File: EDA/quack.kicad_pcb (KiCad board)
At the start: 2 copper layers, 56.6 x 57.7 mm, 39 parts, among them IC1 ESP32-PICO-D4, IC2 SN74LVC4245APWR, J1 DIN-4, J2 DB9_Male, J3 FTDI, J4 MODE, U1 AMS1117-3.3, U2 74LVC2T45DC

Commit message: PCB version 1.3
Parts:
- removed J4: MODE, Connector_PinHeader_2.54mm:PinHeader_2x03_P2.54mm_Vertical
- added Q1: LBSS84LT1G, Package_TO_SOT_SMD:SOT-23, F.Cu at (177.5, 101.0)
- added R6: 470, Resistor_SMD:R_0805_2012Metric, F.Cu at (181.0, 97.0)
- added R7: 470, Resistor_SMD:R_0805_2012Metric, F.Cu at (178.5, 97.0)
- added REF**: MountingHole_3.2mm_M3_Pad, MountingHole:MountingHole_3.2mm_M3_Pad, F.Cu at (169.3, 112.2)
- added REF**: MountingHole_3.2mm_M3_Pad, MountingHole:MountingHole_3.2mm_M3_Pad, F.Cu at (141.3, 112.2)
- added REF**: MountingHole_3.2mm_M3_Pad, MountingHole:MountingHole_3.2mm_M3_Pad, F.Cu at (169.3, 84.2)
- added REF**: MountingHole_3.2mm_M3_Pad, MountingHole:MountingHole_3.2mm_M3_Pad, F.Cu at (141.3, 84.2)
- added SW1: SW_DIP_x03, Button_Switch_THT:SW_DIP_SPSTx03_Slide_9.78x9.8mm_W7.62mm_P2.54mm, F.Cu at (180.5, 113.5)
- R1: value 68 -> 82
- R2, R3, R4: value 150 -> 330
- moved FB2 13.8 mm to (155.5, 111.5)
- moved U2 8.32 mm to (177.5, 105.5)
- moved C8 8.06 mm to (181.0, 104.0)
- moved C9 8.06 mm to (174.0, 104.0)
- moved TP1 7.91 mm to (169.5, 104.5)
- moved R3 3.00 mm to (171.5, 119.0)
- moved FB1 3.00 mm to (166.5, 119.1)
- moved R2 3.00 mm to (169.0, 119.1)
- moved C6 2.00 mm to (174.0, 97.0)
- moved FB3 1.46 mm to (153.0, 111.5), turned to 270 degrees
- moved G*** 0.50 mm to (144.0, 121.5)
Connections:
- IC1 pad 12: ADBSRC -> ~ADBHOST
- IC1 pad 13: BTOFF -> ~BTDIS
- IC1 pad 23: FLASH -> ~FLASH
- IC2 pad 21: GND -> ~ADBHOST
- IC2 pad 3: (no net) -> /quack_connectors/~ADBPULL
- U2 pad 4: (no net) -> GND
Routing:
- net BTOFF: track 90.1 -> 0.00 mm, vias 1 -> 0
- net ~BTDIS: track 0.00 -> 87.2 mm, vias 0 -> 1
- net ~ADBHOST: track 0.00 -> 47.8 mm, vias 0 -> 2
- net ADBSRC: track 38.6 -> 0.00 mm, vias 3 -> 0
- net ~FLASH: track 0.00 -> 28.8 mm, vias 0 -> 1
- net FLASH: track 25.8 -> 0.00 mm, vias 1 -> 0
- net +5V: track 130.8 -> 151.8 mm
- net Net-(FB1-Pad2): track 12.5 -> 30.8 mm
- net /quack_connectors/~ADBPULL: track 0.00 -> 16.3 mm
- net +3V3: track 127.0 -> 132.1 mm
- net DIR: track 36.8 -> 32.7 mm
- net Net-(Q1-Pad1): track 0.00 -> 3.94 mm
- net Net-(FB3-Pad2): track 7.28 -> 3.96 mm, vias 1 -> 0
- net Net-(IC1-Pad16): track 30.0 -> 26.9 mm
- net Net-(Q1-Pad2): track 0.00 -> 2.90 mm
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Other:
- board text added: "ADB Host"
- board text added: "Bluetooth Disable"
- board text removed: "ADBSrc"
- board text removed: "BTOff"

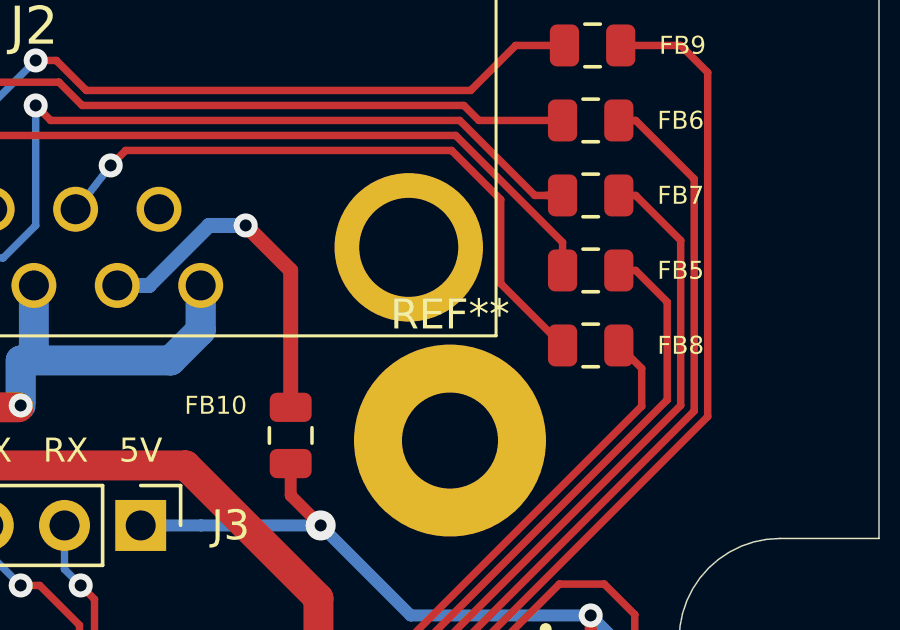
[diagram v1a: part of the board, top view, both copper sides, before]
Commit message: added mounting holes to schematic
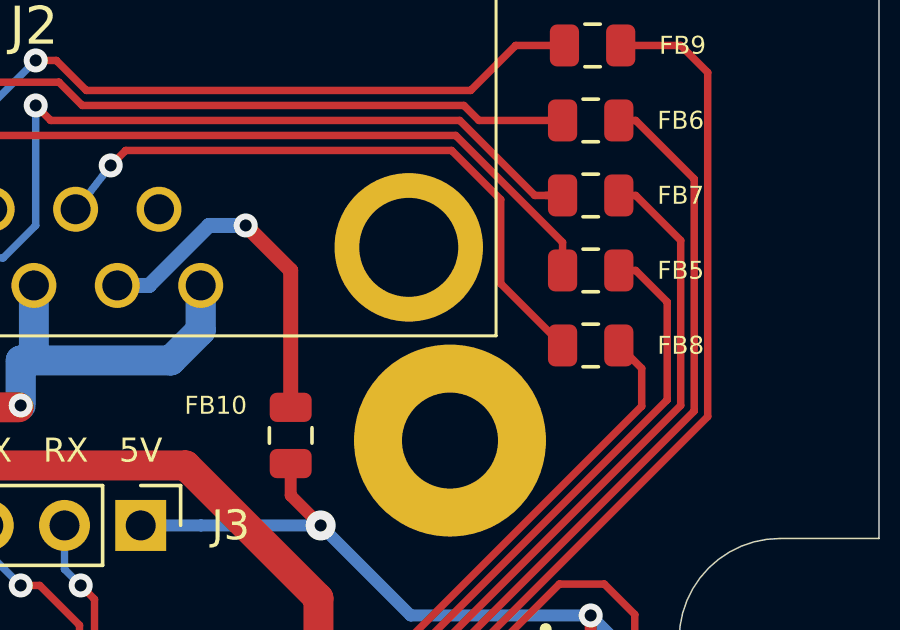
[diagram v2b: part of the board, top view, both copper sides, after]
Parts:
- removed REF** (x4): MountingHole_3.2mm_M3_Pad, MountingHole:MountingHole_3.2mm_M3_Pad
- added H1: M3, MountingHole:MountingHole_3.2mm_M3_Pad, F.Cu at (141.3, 84.2)
- added H2: M3, MountingHole:MountingHole_3.2mm_M3_Pad, F.Cu at (169.3, 84.2)
- added H3: M3, MountingHole:MountingHole_3.2mm_M3_Pad, F.Cu at (141.3, 112.2)
- added H4: M3, MountingHole:MountingHole_3.2mm_M3_Pad, F.Cu at (169.3, 112.2)

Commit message: PCB v1.4
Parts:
- added G***: LOGO, Macintosh logo:Macintosh logo, F.Cu at (132.7, 78.7)
- added H5: 1.152mm, MountingHole_Tooling:MountingHole_1.152mm, F.Cu at (130.2, 120.7)
- added H6: 1.152mm, MountingHole_Tooling:MountingHole_1.152mm, F.Cu at (181.0, 72.4)
- added R8: 22, Resistor_SMD:R_0805_2012Metric, F.Cu at (174.0, 108.0)
- added REF**: OSHW-Logo2_9.8x8mm_Copper, Symbol:OSHW-Logo2_9.8x8mm_Copper, B.Cu at (134.6, 121.3)
- R1: value 82 -> 150
- R2, R3, R4: value 330 -> 470
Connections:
- U2 pad 7: Net-(FB1-Pad2) -> Net-(R8-Pad2)
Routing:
- net Net-(R8-Pad2): track 0.00 -> 11.0 mm, vias 0 -> 2
- net Net-(FB1-Pad2): track 30.8 -> 37.2 mm
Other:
- board text added: "Michel "demik" Depeige :: 68kmla"
- board text added: "Quack Mouse Adapter REV 1.4"
- board text removed: "Michel "demik" Depeige 68kmla"
- board text removed: "Quack Mouse Adapter REV 1.3"

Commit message: fixed R1 and R4 values
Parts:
- R1: value 150 -> 470
- R4: value 470 -> 1200
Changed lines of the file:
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@@
   (title_block
     (title "Quack Mouse Adapter")
-    (date 2021-06-08)
+    (date 2021-08-15)
     (rev 1.4)
     (company Lostwave)
@@
       (effects (font (size 0.6 0.6) (thickness 0.15)))
     )
-    (fp_text value 150 (at 0 1.65 90) (layer F.Fab)
+    (fp_text value 470 (at 0 1.65 90) (layer F.Fab)
       (effects (font (size 1 1) (thickness 0.15)))
     )
@@
       (effects (font (size 0.6 0.6) (thickness 0.15)))
     )
-    (fp_text value 470 (at 0 1.65 90) (layer F.Fab)
-      (effects (font (size 1 1) (thickness 0.15)))
-    )
+    (fp_text value 1200 (at 0 1.65 90) (layer F.Fab)
+      (effects (font (size 1 1) (thickness 0.15)))
+    )

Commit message: PCB v1.5
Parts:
- removed IC1: ESP32-PICO-D4, ESP32-PICO-D4:ESP32-PICO-D4_1
- removed IC2: SN74LVC4245APWR, Package_SO:TSSOP-24_4.4x7.8mm_P0.65mm
- removed the REF** at (134.6, 121.3)
- added REF**: OSHW-Logo2_7.3x6mm_Copper, Symbol:OSHW-Logo2_7.3x6mm_Copper, B.Cu at (131.8, 111.2)
- added TP2: TestPoint DIR ESP32, TestPoint:TestPoint_Pad_1.0x1.0mm, F.Cu at (163.2, 97.0)
- added U3: ESP32-PICO-V3, Package_DFN_QFN:QFN-48-1EP_7x7mm_P0.5mm_EP5.3x5.3mm, F.Cu at (156.2, 97.8)
- added U4: SN74LVC4245APWR, Package_SO:TSSOP-24_4.4x7.8mm_P0.65mm, F.Cu at (168.5, 95.0)
- D1: value BLUE LED -> KT-0805B; footprint LED_SMD:LED_0805_2012Metric_Castellated -> LED_SMD:LED_0805_2012Metric
- D2: value YELLOW LED -> KT-0805Y; footprint LED_SMD:LED_0805_2012Metric_Castellated -> LED_SMD:LED_0805_2012Metric
- D3: value RED LED -> NCD0805R1; footprint LED_SMD:LED_0805_2012Metric_Castellated -> LED_SMD:LED_0805_2012Metric
- D4: value GREEN LED -> KT-0805G; footprint LED_SMD:LED_0805_2012Metric_Castellated -> LED_SMD:LED_0805_2012Metric
- FB1, FB2, FB3: value Ferrite_Bead -> GZ2012D601TF
- FB10, FB4, FB5, FB6, FB7, FB8, FB9: value Ferrite_Bead_Small -> GZ2012D601TF
- Q1: value LBSS84LT1G -> SI2301CDS-T1-GE3
- R1, R2, R3, R6, R7: value 470 -> 470Ω
- R4: value 1200 -> 1.5kΩ
- R5: value 10k -> 10kΩ
- R8: value 22 -> 22Ω
- U2: value 74LVC2T45DC -> SN74LVC2T45YZP; footprint Package_SO:VSSOP-8_2.3x2mm_P0.5mm -> Package_BGA:Texas_DSBGA-8_0.9x1.9mm_Layout2x4_P0.5mm
- moved G*** 0.25 mm to (144.0, 121.2)
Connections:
- C2 pad 1: +3V3 -> +3.3V
- C3 pad 1: +3V3 -> +3.3V
- C4 pad 1: +3V3 -> +3.3V
- C6 pad 1: +3V3 -> +3.3V
- C9 pad 2: +3V3 -> +3.3V
- J1 pad 2: (no net) -> unconnected-(J1-Pad2)
- J2 pad 6: (no net) -> unconnected-(J2-Pad6)
- R5 pad 1: +3V3 -> +3.3V
- R6 pad 2: /quack_connectors/~ADBPULL -> /quack_connectors/~{ADBPULL}
- R8 pad 2: Net-(R8-Pad2) -> Net-(U2-B1)
- SW1 pad 1: ~FLASH -> ~{FLASH}
- SW1 pad 2: ~BTDIS -> ~{BTDIS}
- SW1 pad 3: ~ADBHOST -> ~{ADBHOST}
- U1 pad 2: +3V3 -> +3.3V
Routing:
- net +3.3V: track 0.00 -> 132.6 mm, vias 0 -> 7
- net +3V3: track 132.1 -> 0.00 mm, vias 7 -> 0
- net ~BTDIS: track 87.2 -> 0.00 mm, vias 1 -> 0
- net ~{BTDIS}: track 0.00 -> 84.5 mm, vias 0 -> 1
- net ~ADBHOST: track 47.8 -> 0.00 mm, vias 2 -> 0
- net ~{ADBHOST}: track 0.00 -> 47.6 mm, vias 0 -> 2
- net ~{FLASH}: track 0.00 -> 32.4 mm, vias 0 -> 1
- net ~FLASH: track 28.8 -> 0.00 mm, vias 1 -> 0
- net ~OE: track 19.9 -> 0.00 mm
- net ~{OE}: track 0.00 -> 19.4 mm
- net /quack_connectors/~{ADBPULL}: track 0.00 -> 16.3 mm
- net /quack_connectors/~ADBPULL: track 16.3 -> 0.00 mm
- net Net-(R8-Pad2): track 11.0 -> 0.00 mm, vias 2 -> 0
- net Net-(U2-B1): track 0.00 -> 10.1 mm, vias 0 -> 2
- net Net-(Q1-D): track 37.2 -> 28.4 mm
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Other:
- net class +V removed
- net class Default removed
- net class GND removed
- rule pad_to_mask_clearance: 0.051 -> 0
- board text added: "Quack Mouse Adapter REV 1.5Q"
- board text removed: "Quack Mouse Adapter REV 1.4"
- board text removed: "•"

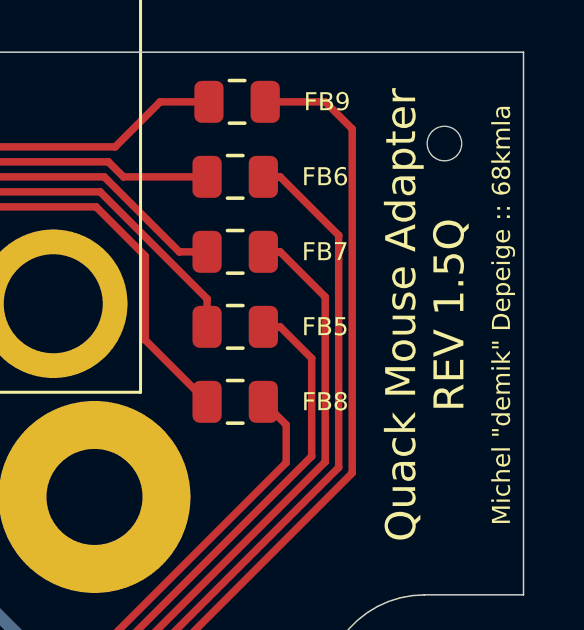
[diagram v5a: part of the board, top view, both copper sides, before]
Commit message: reverted PCB revision to 1.5
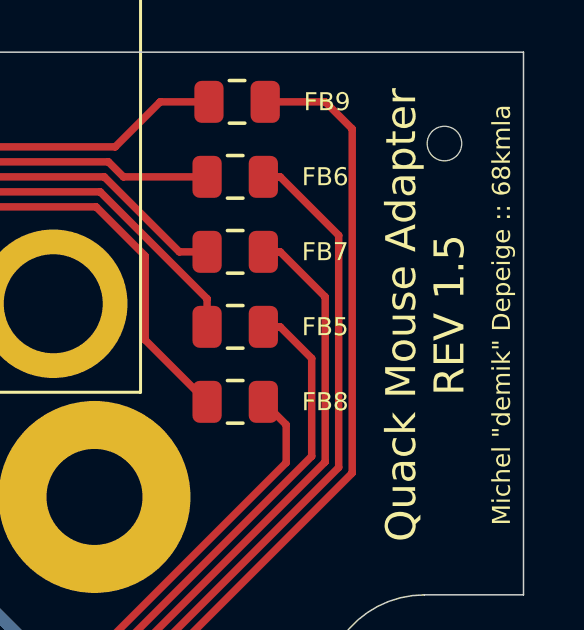
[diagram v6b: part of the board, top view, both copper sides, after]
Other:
- board text added: "Quack Mouse Adapter REV 1.5"
- board text removed: "Quack Mouse Adapter REV 1.5Q"
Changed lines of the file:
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@@
 		)
 	)
-	(gr_text "Quack Mouse Adapter\nREV 1.5Q"
+	(gr_text "Quack Mouse Adapter\nREV 1.5"
 		(at 180.34 78.105 90)
 		(layer "F.SilkS")

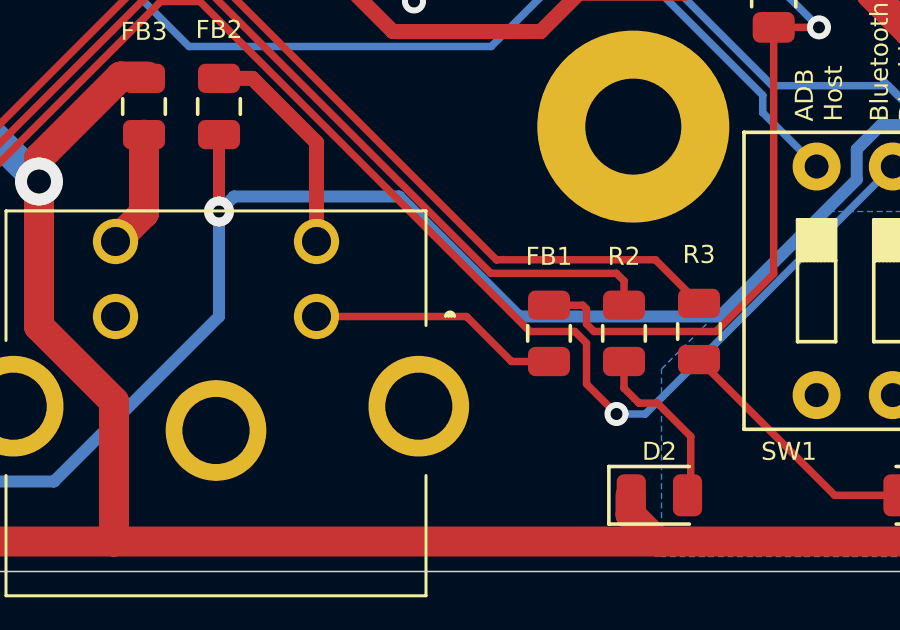
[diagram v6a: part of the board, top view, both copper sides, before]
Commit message: EDA lib: updated Mini DIN 4 connector
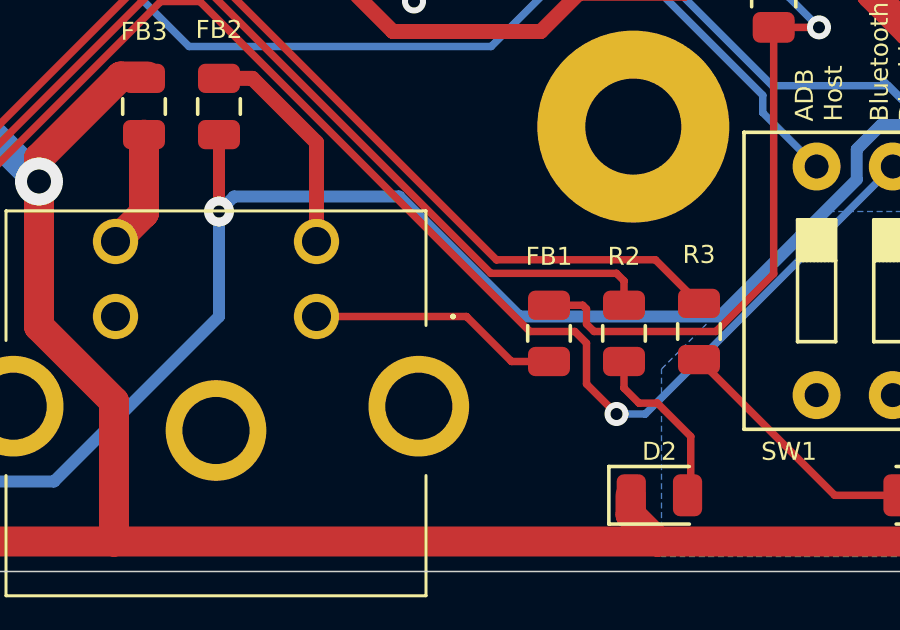
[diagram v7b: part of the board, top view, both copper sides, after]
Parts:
- J1: footprint Quack_MDIN4:57491811 -> Quack_MDIN4:5749181-1
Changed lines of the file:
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@@
 			)
 		)
-		(property "Datasheet" ""
+		(property "Datasheet" "~"
 			(at 0 0 270)
 			(layer "F.Fab")
@@
 		(embedded_fonts no)
 	)
-	(footprint "Quack_MDIN4:57491811"
+	(footprint "Quack_MDIN4:5749181-1"
 		(layer "F.Cu")
 		(at 158.75 118.5)
@@
 		(tags "Connector")
 		(property "Reference" "J1"
-			(at -3.35 0.75 0)
+			(at -3.25 0 0)
 			(layer "F.SilkS")
 			(hide yes)
@@
 		)
 		(fp_arc
-			(start 4.3 0)
-			(mid 4.45 -0.15)
+			(start 4.5 0)
+			(mid 4.55 -0.05)
 			(end 4.6 0)
 			(stroke
@@
 		)
 		(fp_arc
-			(start 4.4 0)
-			(mid 4.45 -0.05)
+			(start 4.6 0)
+			(mid 4.55 0.05)
 			(end 4.5 0)
 			(stroke
@@
 				(type solid)
 			)
-			(layer "Dwgs.User")
+			(layer "F.CrtYd")
 		)
 		(fp_line
@@
 				(type solid)
 			)
-			(layer "Dwgs.User")
+			(layer "F.CrtYd")
+		)
+		(fp_line
+			(start 6.088 -4.52)
+			(end -12.788 -4.52)
+			(stroke
+				(width 0.1)
+				(type solid)
+			)
+			(layer "F.CrtYd")
+		)
+		(fp_line
+			(start 6.088 10.31)
+			(end 6.088 -4.52)
+			(stroke
+				(width 0.1)
+				(type solid)
+			)
+			(layer "F.CrtYd")
 		)
 		(fp_line
@@
 				(type solid)
 			)
-			(layer "Dwgs.User")
+			(layer "F.Fab")
 		)
 		(fp_line
@@
 				(type solid)
 			)
-			(layer "Dwgs.User")
+			(layer "F.Fab")
 		)
 		(fp_line
@@
 				(type solid)
 			)
-			(layer "Dwgs.User")
+			(layer "F.Fab")
 		)
 		(fp_line
@@
 				(type solid)
 			)
-			(layer "Dwgs.User")
-		)
-		(fp_line
-			(start 6.088 -4.52)
-			(end -12.788 -4.52)
-			(stroke
-				(width 0.1)
-				(type solid)
-			)
-			(layer "Dwgs.User")
+			(layer "F.Fab")
 		)
-		(fp_line
-			(start 6.088 10.31)
-			(end 6.088 -4.52)
-			(stroke
-				(width 0.1)
-				(type solid)
+		(fp_text user "${REFERENCE}"
+			(at -3.35 2.895 0)
+			(layer "F.Fab")
+			(effects
+				(font
+					(size 1.27 1.27)
+					(thickness 0.254)
+				)
 			)
-			(layer "Dwgs.User")
 		)
 		(pad "1" thru_hole circle
-			(at 0 0 90)
+			(at 0 0)
 			(size 1.509 1.509)
 			(drill 0.97)
-			(layers "*.Cu" "*.Mask" "F.SilkS")
+			(layers "*.Cu" "*.Mask")
 			(remove_unused_layers no)
 			(net 20 "Net-(FB1-Pad1)")
@@
 		)
 		(pad "2" thru_hole circle
-			(at -6.7 0 90)
+			(at -6.7 0)
 			(size 1.509 1.509)
 			(drill 0.97)
-			(layers "*.Cu" "*.Mask" "F.SilkS")
+			(layers "*.Cu" "*.Mask")
 			(remove_unused_layers no)
 			(net 39 "unconnected-(J1-Pad2)")
@@
 		)
 		(pad "3" thru_hole circle
-			(at 0 -2.5 90)
+			(at 0 -2.5)
 			(size 1.509 1.509)
 			(drill 0.97)
-			(layers "*.Cu" "*.Mask" "F.SilkS")
+			(layers "*.Cu" "*.Mask")
 			(remove_unused_layers no)
 			(net 22 "Net-(FB2-Pad2)")
@@
 		)
 		(pad "4" thru_hole circle
-			(at -6.7 -2.5 90)
+			(at -6.7 -2.5)
 			(size 1.509 1.509)
 			(drill 0.97)
-			(layers "*.Cu" "*.Mask" "F.SilkS")
+			(layers "*.Cu" "*.Mask")
 			(remove_unused_layers no)
 			(net 23 "Net-(FB3-Pad2)")
@@
 		)
 		(pad "MH1" thru_hole circle
-			(at -3.35 3.8 90)
+			(at -3.35 3.8)
 			(size 3.356 3.356)
 			(drill 2.237)
-			(layers "*.Cu" "*.Mask" "F.SilkS")
+			(layers "*.Cu" "*.Mask")
 			(remove_unused_layers no)
 		)
 		(pad "MH2" thru_hole circle
-			(at -10.11 2.99 90)
+			(at -10.11 2.99)
 			(size 3.356 3.356)
 			(drill 2.237)
-			(layers "*.Cu" "*.Mask" "F.SilkS")
+			(layers "*.Cu" "*.Mask")
 			(remove_unused_layers no)
 		)
 		(pad "MH3" thru_hole circle
-			(at 3.41 2.99 90)
+			(at 3.41 2.99)
 			(size 3.356 3.356)
 			(drill 2.237)
-			(layers "*.Cu" "*.Mask" "F.SilkS")
+			(layers "*.Cu" "*.Mask")
 			(remove_unused_layers no)
 		)
 		(embedded_fonts no)
-		(model "${KIPRJMOD}/lib/5749181-1.stp"
+		(model "5749181-1.stp"
 			(offset
-				(xyz -3.25 -8.5 6.5)
-			)
-			(scale
-				(xyz 1 1 1)
-			)
-			(rotate
-				(xyz -90 0 0)
-			)
-		)
-		(model "${KIPRJMOD}/lib/5749181-1.wrl"
-			(offset
-				(xyz -3.25 -8.5 6.5)
+				(xyz -3.349999854 -8.539999834 6.559999844)
 			)
 			(scale
@@
 			)
 		)
-		(property "Datasheet" ""
+		(property "Datasheet" "~"
 			(at 0 0 270)
 			(layer "F.Fab")
@@
 			)
 		)
-		(property "Description" ""
+		(property "Description" "P-MOSFET transistor, gate/source/drain"
 			(at 0 0 270)
 			(layer "F.Fab")

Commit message: update PCB to use Quack_logo.pretty
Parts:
- G***: footprint Macintosh logo:Macintosh logo -> Quack_logo:Macintosh logo
- G***: footprint ADB_logo_5mm:ADB_logo_5mm -> Quack_logo:ADB_logo_5mm
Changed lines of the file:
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@@
 		(embedded_fonts no)
 	)
-	(footprint "Macintosh logo:Macintosh logo"
+	(footprint "Quack_logo:Macintosh logo"
 		(layer "F.Cu")
 		(at 132.75 78.75)
@@
 		(embedded_fonts no)
 	)
-	(footprint "ADB_logo_5mm:ADB_logo_5mm"
+	(footprint "Quack_logo:ADB_logo_5mm"
 		(layer "F.Cu")
 		(at 144 121.25)
